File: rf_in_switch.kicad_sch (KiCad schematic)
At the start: 7 parts, among them P17 CONUFL001-SMD-T, P18 CONUFL001-SMD-T, U31 QPC1022TR7, U32 QPC1022TR7

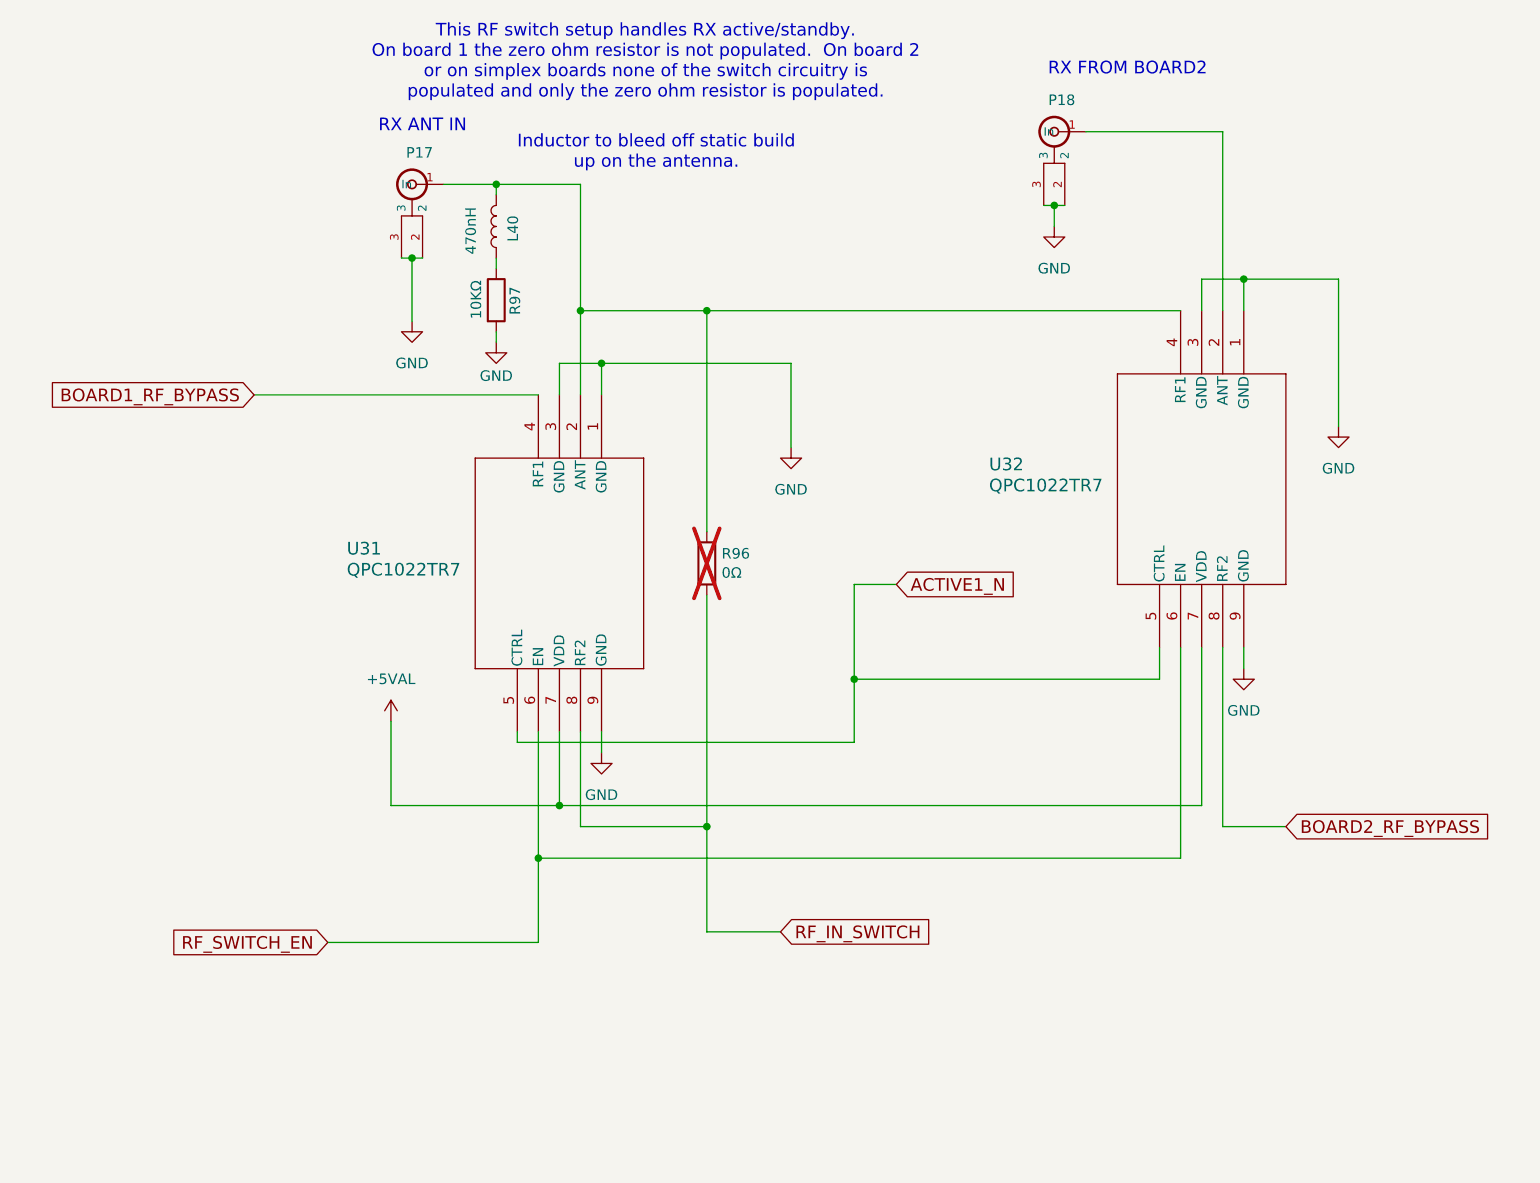
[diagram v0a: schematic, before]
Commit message: Fix a bug in the RF switch circuitry
The board bypass circuitry had an error, the board1 in and antenna
connections were flipped on the switch.  Put them in the right place.

Signed-off-by: Corey Minyard <corey@minyard.net>
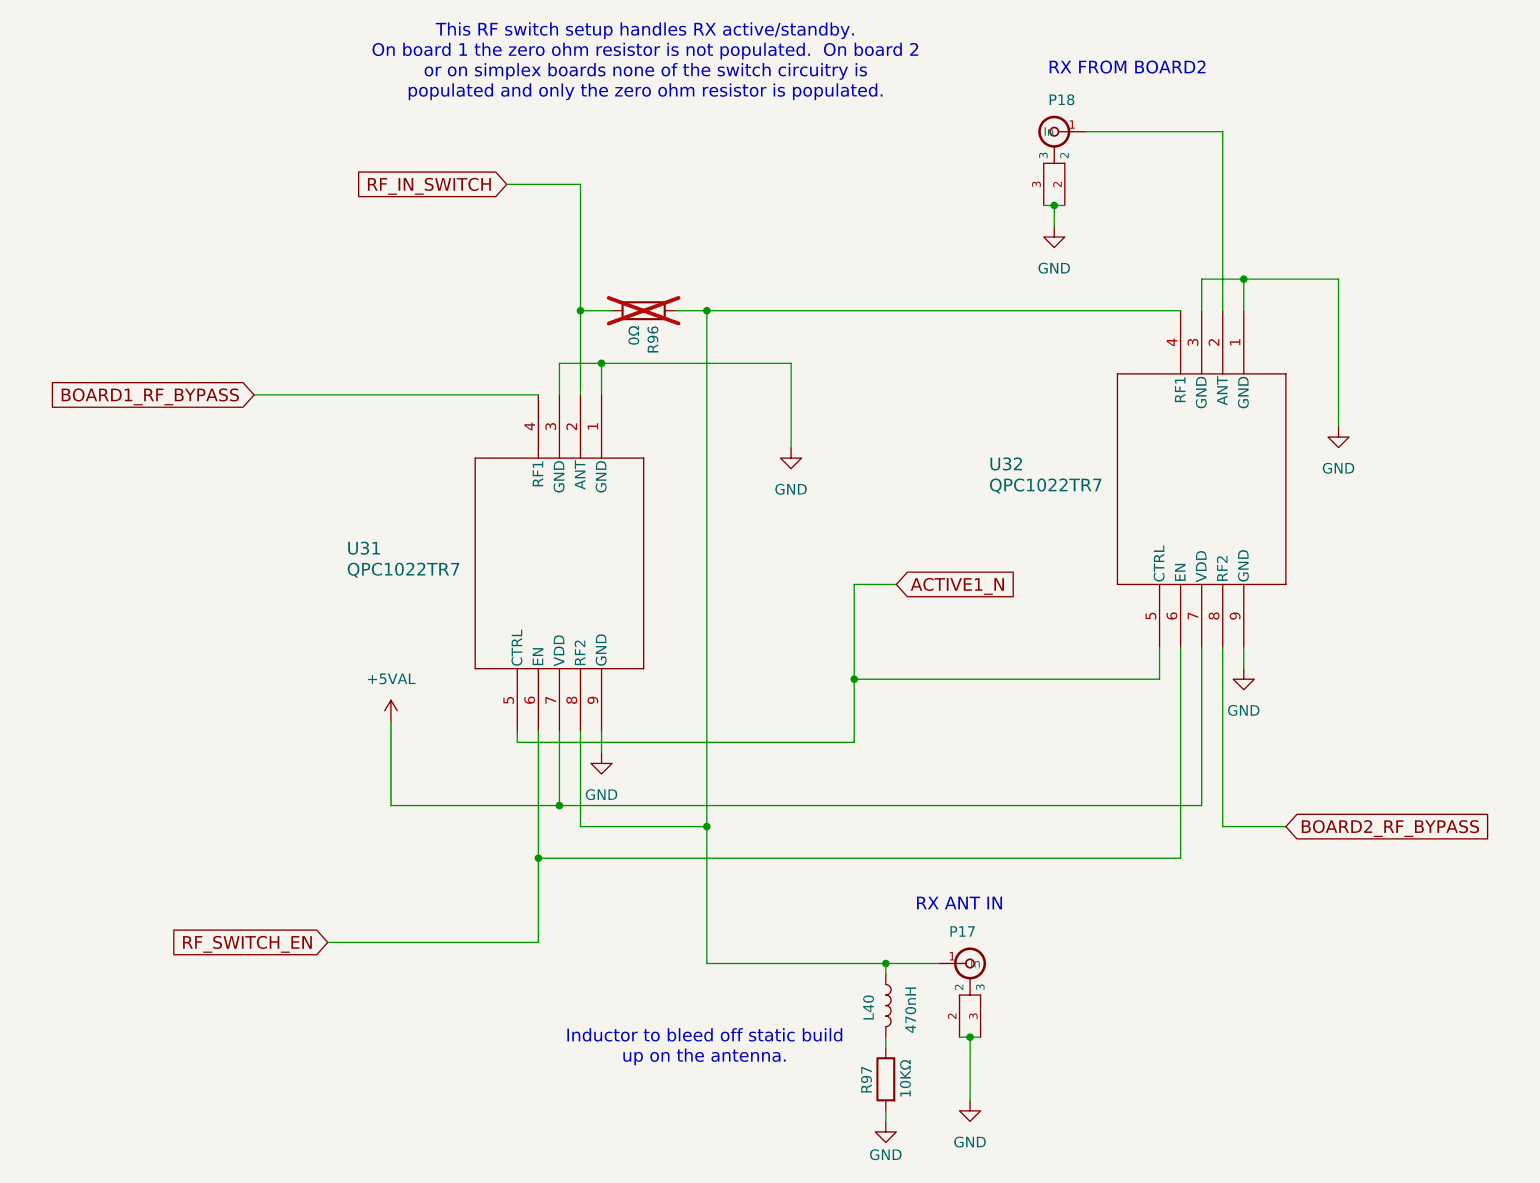
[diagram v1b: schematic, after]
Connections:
- net RF_IN_SWITCH: now also U31.2 (ANT); no longer U31.8 (RF2)
- net at L40.1, P17.1 (In), R96.1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: now also U31.8 (RF2); no longer U31.2 (ANT)
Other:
- moved on the sheet: L40, P17, R96, R97

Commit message: Combine the board bypasses
They are not both used at once, so you can use the same one for both
bypasses.

Signed-off-by: Corey Minyard <corey@minyard.net>
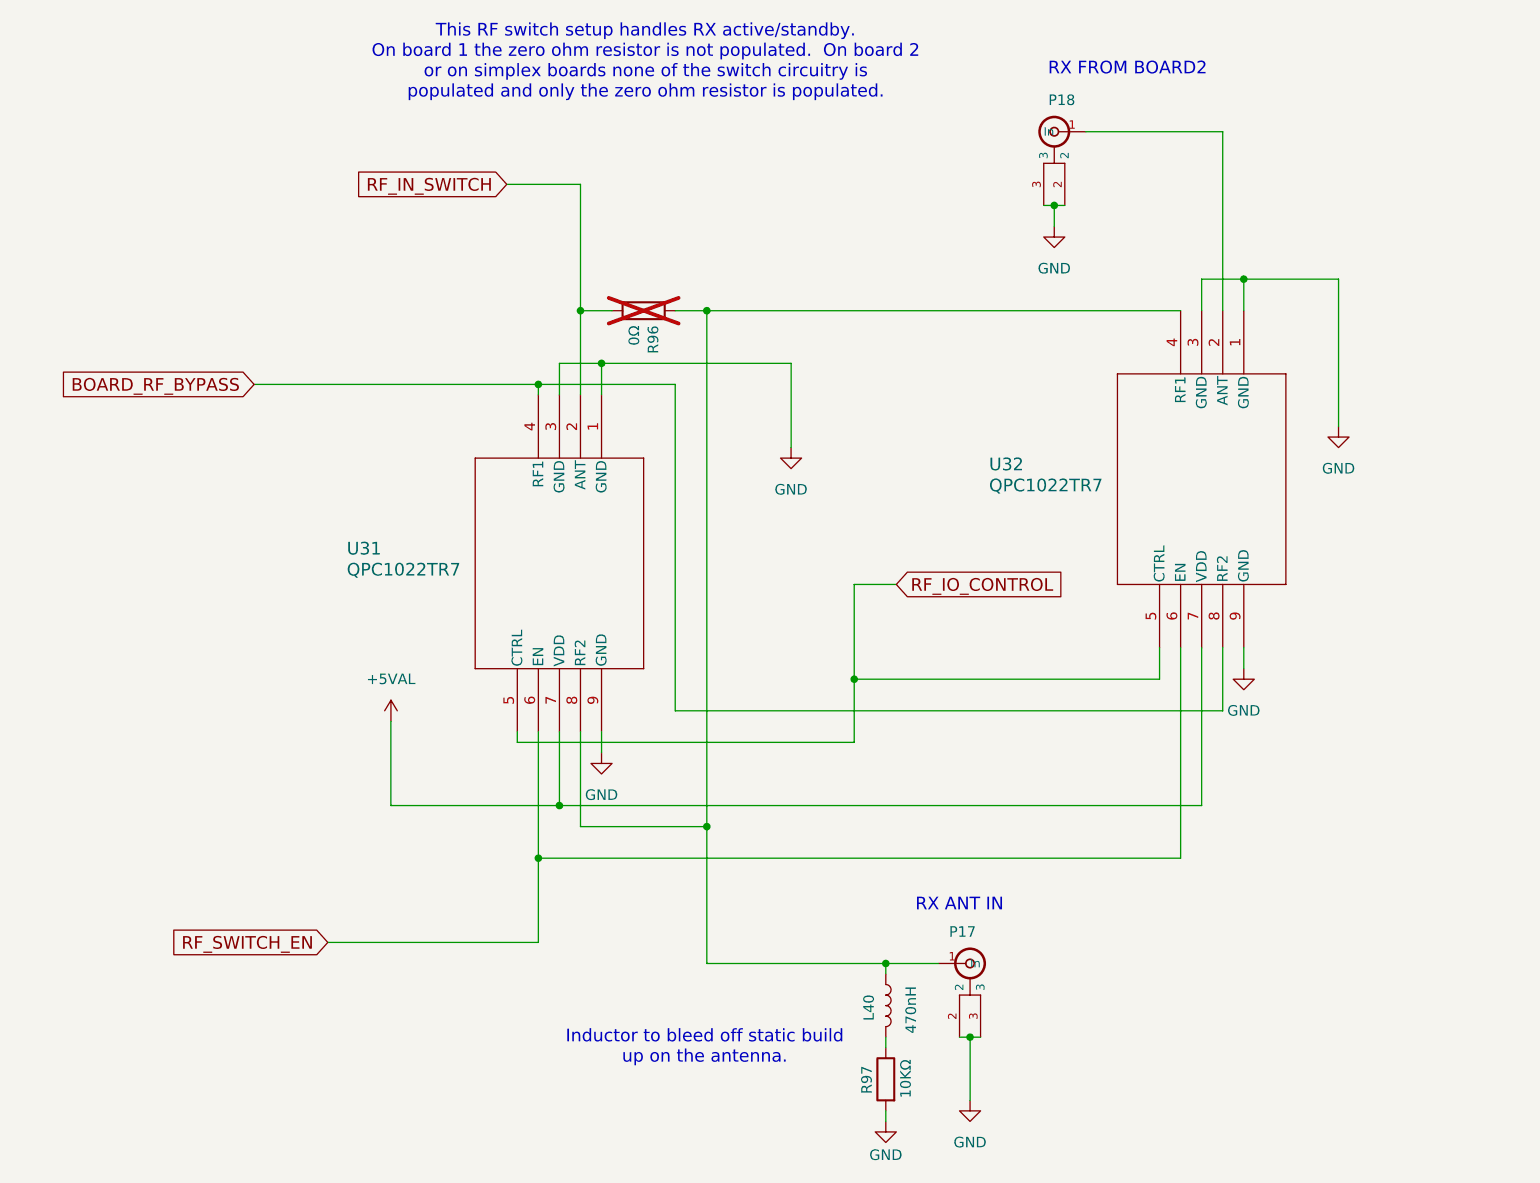
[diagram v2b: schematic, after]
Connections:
- net BOARD2_RF_BYPASS is gone; now on net BOARD_RF_BYPASS: U32.8 (RF2)
- net ACTIVE1_N renamed RF_IO_CONTROL
- net BOARD1_RF_BYPASS renamed BOARD_RF_BYPASS
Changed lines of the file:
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@@
+	)
+	(junction
+		(at 101.6 77.47)
+		(diameter 0)
+		(color 0 0 0 0)
 	)
 	(junction
@@
 	(wire
 		(pts
-			(xy 191.77 130.81) (xy 184.15 130.81)
-		)
-		(stroke
-			(width 0)
-			(type default)
-		)
-	)
-	(wire
-		(pts
 			(xy 186.69 68.58) (xy 186.69 64.77)
 		)
@@
 	(wire
 		(pts
-			(xy 67.31 78.74) (xy 101.6 78.74)
+			(xy 67.31 77.47) (xy 101.6 77.47)
 		)
 		(stroke
@@
 	(wire
 		(pts
+			(xy 118.11 116.84) (xy 184.15 116.84)
+		)
+		(stroke
+			(width 0)
+			(type default)
+		)
+	)
+	(wire
+		(pts
 			(xy 121.92 68.58) (xy 121.92 130.81)
 		)
@@
 	(wire
 		(pts
-			(xy 184.15 109.22) (xy 184.15 130.81)
+			(xy 184.15 109.22) (xy 184.15 116.84)
 		)
 		(stroke
@@
 	(wire
 		(pts
+			(xy 118.11 77.47) (xy 118.11 116.84)
+		)
+		(stroke
+			(width 0)
+			(type default)
+		)
+	)
+	(wire
+		(pts
+			(xy 101.6 77.47) (xy 118.11 77.47)
+		)
+		(stroke
+			(width 0)
+			(type default)
+		)
+	)
+	(wire
+		(pts
+			(xy 101.6 77.47) (xy 101.6 78.74)
+		)
+		(stroke
+			(width 0)
+			(type default)
+		)
+	)
+	(wire
+		(pts
 			(xy 153.67 156.21) (xy 154.94 156.21)
 		)
@@
 			(width 0)
 			(type default)
-		)
-	)
-	(global_label "BOARD2_RF_BYPASS"
-		(shape input)
-		(at 191.77 130.81 0)
-		(fields_autoplaced yes)
-		(effects
-			(font
-				(size 1.524 1.524)
-			)
-			(justify left)
-		)
-		(property "Intersheetrefs" "${INTERSHEET_REFS}"
-			(at 217.209 130.81 0)
-			(effects
-				(font
-					(size 1.27 1.27)
-				)
-				(justify left)
-				(hide yes)
-			)
 		)
 	)
@@
 		)
 	)
-	(global_label "ACTIVE1_N"
+	(global_label "RF_IO_CONTROL"
 		(shape input)
 		(at 144.78 101.6 0)
@@
 		)
 		(property "Intersheetrefs" "${INTERSHEET_REFS}"
-			(at 159.1882 101.6 0)
+			(at 165.2842 101.6 0)
 			(effects
 				(font
@@
 		)
 	)
-	(global_label "BOARD1_RF_BYPASS"
+	(global_label "BOARD_RF_BYPASS"
 		(shape input)
-		(at 67.31 78.74 180)
+		(at 67.31 77.47 180)
 		(fields_autoplaced yes)
 		(effects
@@
 		)
 		(property "Intersheetrefs" "${INTERSHEET_REFS}"
-			(at 41.871 78.74 0)
+			(at 43.3224 77.47 0)
 			(effects
 				(font

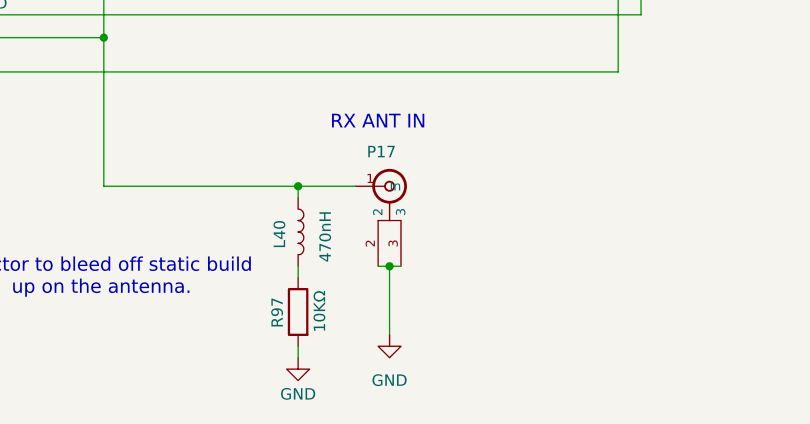
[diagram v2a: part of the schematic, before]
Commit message: Convert main TX/RX connectors to MMCX
That's what is more standard, and it has more insertion/removal cycles
than U.FL.

Signed-off-by: Corey Minyard <corey@minyard.net>
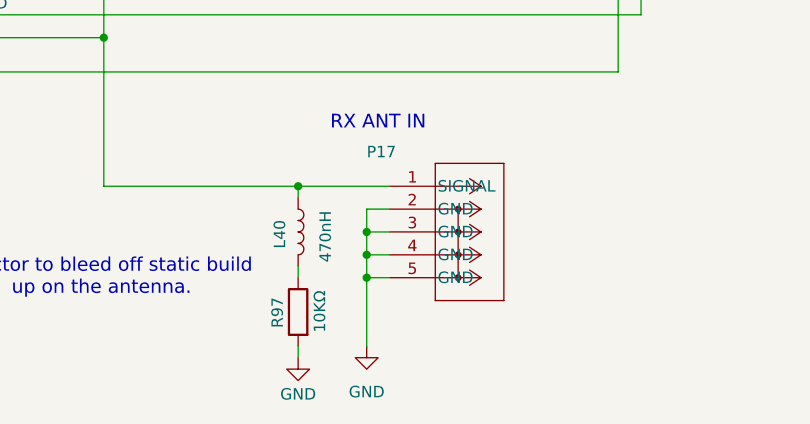
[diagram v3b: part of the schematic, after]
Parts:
- P17: footprint PacSatDev_misc:CONN1_CONUFL_TEC -> PacSatDev_misc:COAX4_MMCX-J-P-H-ST-TH1_SAI; symbol PACSAT_DEV_misc:U_FL -> PACSAT_DEV_misc:MMCX-J-P-H-ST-TH1
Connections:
- net GND: now also P17.4 (GND), P17.5 (GND)
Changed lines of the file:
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@@
+	)
+	(junction
+		(at 151.13 154.94)
+		(diameter 0)
+		(color 0 0 0 0)
 	)
 	(junction
@@
 	)
 	(junction
+		(at 151.13 152.4)
+		(diameter 0)
+		(color 0 0 0 0)
+	)
+	(junction
 		(at 121.92 68.58)
 		(diameter 0)
@@
 	)
 	(junction
-		(at 153.67 156.21)
+		(at 151.13 157.48)
 		(diameter 0)
 		(color 0 0 0 0)
@@
 	(wire
 		(pts
+			(xy 151.13 152.4) (xy 151.13 154.94)
+		)
+		(stroke
+			(width 0)
+			(type default)
+		)
+	)
+	(wire
+		(pts
 			(xy 181.61 109.22) (xy 181.61 128.27)
 		)
@@
 	(wire
 		(pts
-			(xy 153.67 156.21) (xy 153.67 163.83)
+			(xy 151.13 149.86) (xy 151.13 152.4)
 		)
 		(stroke
@@
 	(wire
 		(pts
+			(xy 151.13 157.48) (xy 151.13 165.1)
+		)
+		(stroke
+			(width 0)
+			(type default)
+		)
+	)
+	(wire
+		(pts
 			(xy 163.83 55.88) (xy 165.1 55.88)
 		)
@@
 	(wire
 		(pts
+			(xy 151.13 154.94) (xy 151.13 157.48)
+		)
+		(stroke
+			(width 0)
+			(type default)
+		)
+	)
+	(wire
+		(pts
 			(xy 104.14 128.27) (xy 83.82 128.27)
 		)
@@
 	(wire
 		(pts
-			(xy 149.86 147.32) (xy 143.51 147.32)
+			(xy 143.51 147.32) (xy 153.67 147.32)
 		)
 		(stroke
@@
 	(wire
 		(pts
-			(xy 153.67 156.21) (xy 152.4 156.21)
-		)
-		(stroke
-			(width 0)
-			(type default)
-		)
-	)
-	(wire
-		(pts
 			(xy 143.51 156.21) (xy 143.51 157.48)
 		)
@@
 	(wire
 		(pts
+			(xy 151.13 157.48) (xy 153.67 157.48)
+		)
+		(stroke
+			(width 0)
+			(type default)
+		)
+	)
+	(wire
+		(pts
 			(xy 83.82 118.11) (xy 83.82 128.27)
 		)
@@
 	(wire
 		(pts
+			(xy 151.13 149.86) (xy 153.67 149.86)
+		)
+		(stroke
+			(width 0)
+			(type default)
+		)
+	)
+	(wire
+		(pts
 			(xy 118.11 68.58) (xy 121.92 68.58)
 		)
@@
 	(wire
 		(pts
+			(xy 151.13 152.4) (xy 153.67 152.4)
+		)
+		(stroke
+			(width 0)
+			(type default)
+		)
+	)
+	(wire
+		(pts
 			(xy 101.6 77.47) (xy 101.6 78.74)
 		)
@@
 	(wire
 		(pts
-			(xy 153.67 156.21) (xy 154.94 156.21)
+			(xy 153.67 154.94) (xy 151.13 154.94)
 		)
 		(stroke
@@
 	)
 	(symbol
-		(lib_id "PACSAT_DEV_misc:U_FL")
+		(lib_id "PACSAT_DEV_misc:MMCX-J-P-H-ST-TH1")
 		(at 153.67 147.32 0)
 		(unit 1)
@@
 			)
 		)
-		(property "Footprint" "PacSatDev_misc:CONN1_CONUFL_TEC"
+		(property "Footprint" "PacSatDev_misc:COAX4_MMCX-J-P-H-ST-TH1_SAI"
 			(at 153.67 147.32 0)
 			(effects
 				(font
 					(size 1.27 1.27)
-				)
-				(hide yes)
-			)
-		)
-		(property "Datasheet" ""
+					(italic yes)
+				)
+				(hide yes)
+			)
+		)
+		(property "Datasheet" "MMCX-J-P-H-ST-TH1"
 			(at 153.67 147.32 0)
 			(effects
 				(font
 					(size 1.27 1.27)
+					(italic yes)
 				)
 				(hide yes)
@@
 					(size 1.27 1.27)
 				)
+				(hide yes)
 			)
 		)
@@
 		)
 		(pin "3"
+		)
+		(pin "5"
+		)
+		(pin "4"
 		)
 		(instances
@@
 	(symbol
 		(lib_id "power:GND")
-		(at 153.67 163.83 0)
+		(at 151.13 165.1 0)
 		(mirror y)
 		(unit 1)
@@
 		(fields_autoplaced yes)
 		(property "Reference" "#PWR0204"
-			(at 153.67 170.18 0)
+			(at 151.13 171.45 0)
 			(effects
 				(font
@@
 		)
 		(property "Value" "GND"
-			(at 153.67 168.91 0)
+			(at 151.13 170.18 0)
 			(effects
 				(font
@@
 		)
 		(property "Footprint" ""
-			(at 153.67 163.83 0)
+			(at 151.13 165.1 0)
 			(effects
 				(font
@@
 		)
 		(property "Datasheet" ""
-			(at 153.67 163.83 0)
+			(at 151.13 165.1 0)
 			(effects
 				(font
@@
 		)
 		(property "Description" ""
-			(at 153.67 163.83 0)
-			(effects
-				(font
+			(at 151.13 165.1 0)
+			(effects
+				(font
